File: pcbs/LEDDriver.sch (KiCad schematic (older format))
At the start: 1 part, among them J1 Conn_02x32_Counter_Clockwise

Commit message: LED driver part done.
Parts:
- added C1: 10n, Resistors_SMD:R_0603, symbol C
- added C2: 100n, Resistors_SMD:R_0603, symbol C
- added C3: 10u, Resistors_SMD:R_0603, symbol C
- added J2: Conn_02x03_Odd_Even, Pin_Headers:Pin_Header_Straight_2x03_Pitch2.54mm, symbol Conn_02x03_Odd_Even
- added R1, R2: 0R, Resistors_SMD:R_0603, symbol R
- added R3, R4: 10k, Resistors_SMD:R_0603, symbol R
- added RV1: T73YE103KT20, Potis:Vishay_T73YE103KT20, symbol POT
- added U1: DAC101C085, SSOP:VSSOP-8_3.0x3.0mm_Pitch0.65mm, symbol DAC101C085
- J1: footprint (none) -> Pin_Headers:Pin_Header_Straight_2x32_Pitch2.54mm; Samtec (none) -> TSW-132-07-G-D
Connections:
- net LED_N_01: now reaches J1.1 (Pin_1)
- net LED_N_10: now reaches J1.10 (Pin_10)
- net LED_N_11: now reaches J1.11 (Pin_11)
- net LED_N_12: now reaches J1.12 (Pin_12)
- net LED_N_13: now reaches J1.13 (Pin_13)
- net LED_N_14: now reaches J1.14 (Pin_14)
- net LED_N_15: now reaches J1.15 (Pin_15)
- net LED_N_16: now reaches J1.16 (Pin_16)
- net LED_N_17: now reaches J1.17 (Pin_17)
- net LED_N_18: now reaches J1.18 (Pin_18)
- net LED_N_19: now reaches J1.19 (Pin_19)
- net LED_N_02: now reaches J1.2 (Pin_2)
- net LED_N_20: now reaches J1.20 (Pin_20)
- net LED_N_21: now reaches J1.21 (Pin_21)
- net LED_N_22: now reaches J1.22 (Pin_22)
- net LED_N_23: now reaches J1.23 (Pin_23)
- net LED_N_24: now reaches J1.24 (Pin_24)
- net LED_N_25: now reaches J1.25 (Pin_25)
- net LED_N_26: now reaches J1.26 (Pin_26)
- net LED_N_27: now reaches J1.27 (Pin_27)
- net LED_N_28: now reaches J1.28 (Pin_28)
- net LED_N_29: now reaches J1.29 (Pin_29)
- net LED_N_03: now reaches J1.3 (Pin_3)
- net LED_N_30: now reaches J1.30 (Pin_30)
- net LED_N_31: now reaches J1.31 (Pin_31)
- net LED_N_32: now reaches J1.32 (Pin_32)
- net LED_N_33: now reaches J1.33 (Pin_33)
- net LED_N_34: now reaches J1.34 (Pin_34)
- net LED_N_35: now reaches J1.35 (Pin_35)
- net LED_N_36: now reaches J1.36 (Pin_36)
- net LED_N_37: now reaches J1.37 (Pin_37)
- net LED_N_38: now reaches J1.38 (Pin_38)
- net LED_N_39: now reaches J1.39 (Pin_39)
- net LED_N_04: now reaches J1.4 (Pin_4)
- net LED_N_40: now reaches J1.40 (Pin_40)
- net LED_N_41: now reaches J1.41 (Pin_41)
- net LED_N_42: now reaches J1.42 (Pin_42)
- net LED_N_43: now reaches J1.43 (Pin_43)
- net LED_N_44: now reaches J1.44 (Pin_44)
- net LED_N_45: now reaches J1.45 (Pin_45)
- net LED_N_46: now reaches J1.46 (Pin_46)
- net LED_N_47: now reaches J1.47 (Pin_47)
- net LED_N_48: now reaches J1.48 (Pin_48)
- net LED_N_49: now reaches J1.49 (Pin_49)
- net LED_N_05: now reaches J1.5 (Pin_5)
- net LED_N_50: now reaches J1.50 (Pin_50)
- net LED_N_51: now reaches J1.51 (Pin_51)
- net LED_N_52: now reaches J1.52 (Pin_52)
- net LED_N_53: now reaches J1.53 (Pin_53)
- net LED_N_54: now reaches J1.54 (Pin_54)
- net LED_N_55: now reaches J1.55 (Pin_55)
- net LED_N_56: now reaches J1.56 (Pin_56)
- net LED_N_57: now reaches J1.57 (Pin_57)
- net LED_N_58: now reaches J1.58 (Pin_58)
- net LED_N_59: now reaches J1.59 (Pin_59)
- net LED_N_06: now reaches J1.6 (Pin_6)
- net LED_N_60: now reaches J1.60 (Pin_60)
- net LED_N_61: now reaches J1.61 (Pin_61)
- net LED_N_62: now reaches J1.62 (Pin_62)
- net LED_N_63: now reaches J1.63 (Pin_63)
- net LED_N_64: now reaches J1.64 (Pin_64)
- net LED_N_07: now reaches J1.7 (Pin_7)
- net LED_N_08: now reaches J1.8 (Pin_8)
- net LED_N_09: now reaches J1.9 (Pin_9)
- new net: R1.2, U1.1 (ADR0)
- new net: R2.2, U1.2 (ADR1)
- new net: R3.1, RV1.1
- new net: J2.1 (Pin_1), RV1.2
- new net 3V3: C1.1, C2.1, C3.1, R1.1, R2.1, R3.2, U1.6 (VA), U1.7 (VREF)
- new net GND: C1.2, C2.2, C3.2, J2.5 (Pin_5), R4.2, RV1.3, U1.5 (GND)
- new net I2C_SCL: U1.4 (SDA)
- new net I2C_SDA: U1.3 (SCL)
- new net VDAC: J2.3 (Pin_3), U1.8 (VOUT)
- new net VSIG: J2.2 (Pin_2), J2.4 (Pin_4), J2.6 (Pin_6), R4.1
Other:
- moved on the sheet: J1

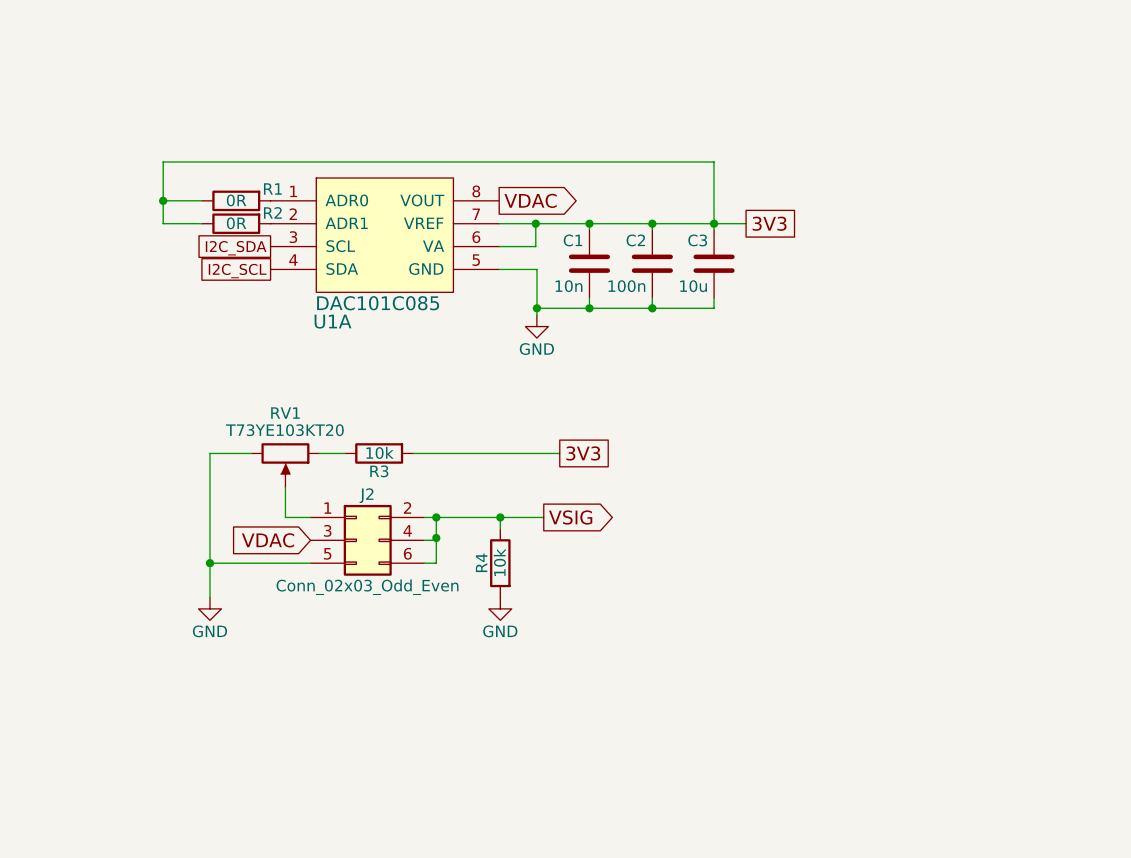
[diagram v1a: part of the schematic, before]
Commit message: Only UI is left for schematics.
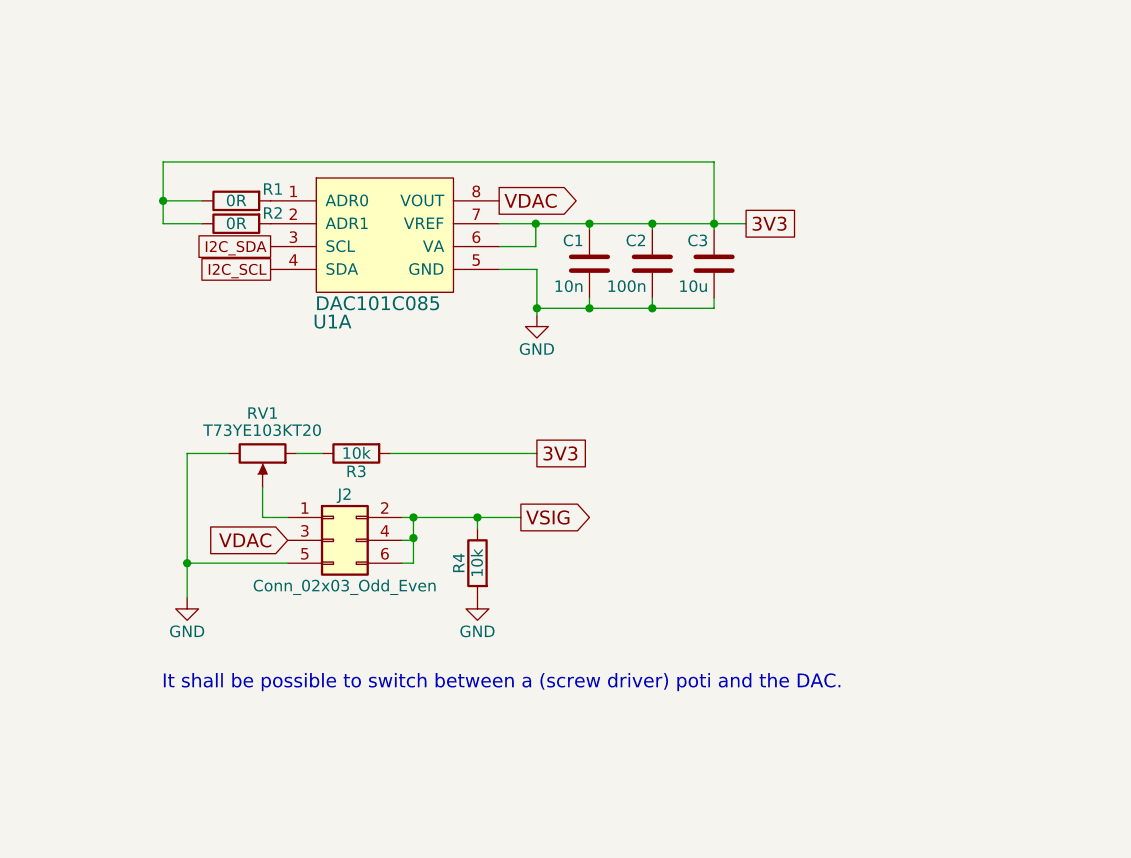
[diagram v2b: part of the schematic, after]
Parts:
- C1: Digikey 490-7194-1-ND -> 311-1085-1-ND
- C2: Digikey 490-5881-1-ND -> 311-1088-1-ND
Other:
- note added: "It shall be possible to switch between a (screw driver) poti and the DAC."
- moved on the sheet: J2, R3, R4, RV1
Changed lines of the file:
@@
 LIBS:myopamps
 LIBS:mydacs
+LIBS:mydcdcs
 LIBS:led_driver-cache
 EELAYER 25 0
@@
 $Descr A4 11693 8268
 encoding utf-8
-Sheet 2 35
+Sheet 2 37
 Title "UV LED Driver with 64 Stages and DAC"
 Date "2017-11-13"
@@
 F 2 "Resistors_SMD:R_0603" H 9733 3150 50  0001 C CNN
 F 3 "" H 9695 3300 50  0000 C CNN
-F 4 "490-5881-1-ND" H 9695 3300 60  0001 C CNN "Digikey"
+F 4 "311-1088-1-ND" H 9695 3300 60  0001 C CNN "Digikey"
 	1    9695 3300
 	-1   0    0    -1
 $EndComp
-$Comp
-L C C1
-U 1 1 5A10F0A2
-P 9420 3300
-F 0 "C1" H 9445 3400 50  0000 L CNN
-F 1 "10n" H 9445 3200 50  0000 L CNN
-F 2 "Resistors_SMD:R_0603" H 9458 3150 50  0001 C CNN
-F 3 "" H 9420 3300 50  0000 C CNN
-F 4 "490-7194-1-ND" H 9420 3300 60  0001 C CNN "Digikey"
-	1    9420 3300
-	-1   0    0    -1
-$EndComp
-Wire Wire Line
-	9025 3125 9185 3125
-Wire Wire Line
-	9185 3125 9420 3125
-Wire Wire Line
-	9420 3125 9695 3125
-Wire Wire Line
-	9695 3125 9965 3125
-Wire Wire Line
-	9965 3125 10105 3125
+Wire Wire Line
+	9025 3125 10105 3125
 Wire Wire Line
 	9695 3125 9695 3150
@@
 	9025 3325 9190 3325
 Wire Wire Line
-	9190 3325 9190 3495
-Wire Wire Line
-	9190 3495 9190 3525
+	9190 3325 9190 3525
 Wire Wire Line
 	9695 3495 9695 3450
 Wire Wire Line
-	9190 3495 9420 3495
-Wire Wire Line
-	9420 3495 9695 3495
-Wire Wire Line
-	9695 3495 9965 3495
+	9190 3495 9965 3495
 Connection ~ 9190 3495
 Wire Wire Line
@@
 Connection ~ 9695 3495
 Wire Wire Line
-	9965 2855 9965 3125
-Wire Wire Line
-	9965 3125 9965 3150
+	9965 2855 9965 3150
 Connection ~ 9965 3125
 Text GLabel 8025 3225 0    47   UnSpc ~ 0
@@
 	7555 3125 7725 3125
 Wire Wire Line
-	7555 2855 7555 3025
-Wire Wire Line
-	7555 3025 7555 3125
+	7555 2855 7555 3125
 Wire Wire Line
 	7725 3025 7555 3025
@@
 L R R3
 U 1 1 5A1370E7
-P 8500 4130
-F 0 "R3" V 8580 4130 50  0000 C CNN
-F 1 "10k" V 8500 4130 50  0000 C CNN
-F 2 "Resistors_SMD:R_0603" V 8430 4130 50  0001 C CNN
-F 3 "" H 8500 4130 50  0001 C CNN
-F 4 "311-10KGRCT-ND" V 8500 4130 60  0001 C CNN "Digikey"
-	1    8500 4130
+P 8400 4130
+F 0 "R3" V 8480 4130 50  0000 C CNN
+F 1 "10k" V 8400 4130 50  0000 C CNN
+F 2 "Resistors_SMD:R_0603" V 8330 4130 50  0001 C CNN
+F 3 "" H 8400 4130 50  0001 C CNN
+F 4 "311-10KGRCT-ND" V 8400 4130 60  0001 C CNN "Digikey"
+	1    8400 4130
 	0    -1   1    0
 $EndComp
-Text GLabel 9290 4130 2    60   UnSpc ~ 0
+Text GLabel 9190 4130 2    60   UnSpc ~ 0
 3V3
 Wire Wire Line
-	8650 4130 9290 4130
-Wire Wire Line
-	8350 4130 8240 4130
-Wire Wire Line
-	8200 4410 8090 4410
-Wire Wire Line
-	8090 4410 8090 4280
+	8550 4130 9190 4130
+Wire Wire Line
+	8250 4130 8140 4130
+Wire Wire Line
+	8100 4410 7990 4410
+Wire Wire Line
+	7990 4410 7990 4280
 $Comp
 L POT RV1
 U 1 1 5A139EFD
-P 8090 4130
-F 0 "RV1" V 7915 4130 50  0000 C CNN
-F 1 "T73YE103KT20" V 7990 4130 50  0000 C CNN
-F 2 "Potis:Vishay_T73YE103KT20" H 8090 4130 50  0001 C CNN
-F 3 "http://www.bourns.com/docs/Product-Datasheets/3362.pdf" H 8090 4130 50  0001 C CNN
-F 4 " 3362R-103LF-ND" V 8090 4130 60  0001 C CNN "Digikey"
-	1    8090 4130
+P 7990 4130
+F 0 "RV1" V 7815 4130 50  0000 C CNN
+F 1 "T73YE103KT20" V 7890 4130 50  0000 C CNN
+F 2 "Potis:Vishay_T73YE103KT20" H 7990 4130 50  0001 C CNN
+F 3 "http://www.bourns.com/docs/Product-Datasheets/3362.pdf" H 7990 4130 50  0001 C CNN
+F 4 " 3362R-103LF-ND" V 7990 4130 60  0001 C CNN "Digikey"
+	1    7990 4130
 	0    1    1    0
 $EndComp
@@
 L GND #PWR1
 U 1 1 5A142088
-P 7760 4760
-F 0 "#PWR1" H 7760 4510 50  0001 C CNN
-F 1 "GND" H 7760 4610 50  0000 C CNN
-F 2 "" H 7760 4760 50  0000 C CNN
-F 3 "" H 7760 4760 50  0000 C CNN
-	1    7760 4760
+P 7660 4760
+F 0 "#PWR1" H 7660 4510 50  0001 C CNN
+F 1 "GND" H 7660 4610 50  0000 C CNN
+F 2 "" H 7660 4760 50  0000 C CNN
+F 3 "" H 7660 4760 50  0000 C CNN
+	1    7660 4760
 	-1   0    0    -1
 $EndComp
-Text GLabel 8200 4510 0    60   Input ~ 0
+Text GLabel 8100 4510 0    60   Input ~ 0
 VDAC
-Text GLabel 9220 4410 2    60   Output ~ 0
+Text GLabel 9120 4410 2    60   Output ~ 0
 VSIG
 Wire Wire Line
-	8700 4410 8750 4410
-Wire Wire Line
-	8750 4410 9030 4410
-Wire Wire Line
-	9030 4410 9220 4410
-Wire Wire Line
-	8750 4510 8700 4510
-Wire Wire Line
-	8750 4410 8750 4500
-Wire Wire Line
-	8750 4500 8750 4510
-Connection ~ 8750 4410
+	8600 4410 9120 4410
+Wire Wire Line
+	8650 4510 8600 4510
+Wire Wire Line
+	8650 4410 8650 4510
+Connection ~ 8650 4410
 $Comp
 L Conn_02x03_Odd_Even J2
 U 1 1 5A1548D7
-P 8400 4510
-F 0 "J2" H 8450 4710 50  0000 C CNN
-F 1 "Conn_02x03_Odd_Even" H 8450 4310 50  0000 C CNN
-F 2 "Pin_Headers:Pin_Header_Straight_2x03_Pitch2.54mm" H 8400 4510 50  0001 C CNN
-F 3 "" H 8400 4510 50  0001 C CNN
-F 4 "TSW-103-07-G-D" H 8400 4510 60  0001 C CNN "Digikey"
-	1    8400 4510
+P 8300 4510
+F 0 "J2" H 8350 4710 50  0000 C CNN
+F 1 "Conn_02x03_Odd_Even" H 8350 4310 50  0000 C CNN
+F 2 "Pin_Headers:Pin_Header_Straight_2x03_Pitch2.54mm" H 8300 4510 50  0001 C CNN
+F 3 "" H 8300 4510 50  0001 C CNN
+F 4 "TSW-103-07-G-D" H 8300 4510 60  0001 C CNN "Digikey"
+	1    8300 4510
 	1    0    0    -1
 $EndComp
 Wire Wire Line
-	8700 4610 8750 4610
-Wire Wire Line
-	8750 4610 8750 4500
-Connection ~ 8750 4500
-Wire Wire Line
-	8200 4610 7760 4610
-Wire Wire Line
-	7760 4130 7760 4610
-Wire Wire Line
-	7760 4610 7760 4760
-Wire Wire Line
-	7760 4130 7940 4130
-Connection ~ 7760 4610
+	8600 4610 8650 4610
+Wire Wire Line
+	8650 4610 8650 4500
+Connection ~ 8650 4500
+Wire Wire Line
+	8100 4610 7660 4610
+Wire Wire Line
+	7660 4130 7660 4760
+Wire Wire Line
+	7660 4130 7840 4130
+Connection ~ 7660 4610
 $Comp
 L R R4
 U 1 1 5A15A992
-P 9030 4610
-F 0 "R4" V 9110 4610 50  0000 C CNN
-F 1 "10k" V 9030 4610 50  0000 C CNN
-F 2 "Resistors_SMD:R_0603" V 8960 4610 50  0001 C CNN
-F 3 "" H 9030 4610 50  0001 C CNN
-F 4 "311-10KGRCT-ND" V 9030 4610 60  0001 C CNN "Digikey"
-	1    9030 4610
+P 8930 4610
+F 0 "R4" V 9010 4610 50  0000 C CNN
+F 1 "10k" V 8930 4610 50  0000 C CNN
+F 2 "Resistors_SMD:R_0603" V 8860 4610 50  0001 C CNN
+F 3 "" H 8930 4610 50  0001 C CNN
+F 4 "311-10KGRCT-ND" V 8930 4610 60  0001 C CNN "Digikey"
+	1    8930 4610
 	-1   0    0    -1
 $EndComp
 Wire Wire Line
-	9030 4460 9030 4410
-Connection ~ 9030 4410
+	8930 4460 8930 4410
+Connection ~ 8930 4410
 $Comp
 L GND #PWR2
 U 1 1 5A15B686
-P 9030 4760
-F 0 "#PWR2" H 9030 4510 50  0001 C CNN
-F 1 "GND" H 9030 4610 50  0000 C CNN
-F 2 "" H 9030 4760 50  0000 C CNN
-F 3 "" H 9030 4760 50  0000 C CNN
-	1    9030 4760
+P 8930 4760
+F 0 "#PWR2" H 8930 4510 50  0001 C CNN
+F 1 "GND" H 8930 4610 50  0000 C CNN
+F 2 "" H 8930 4760 50  0000 C CNN
+F 3 "" H 8930 4760 50  0000 C CNN
+	1    8930 4760
 	-1   0    0    -1
 $EndComp
+Text Notes 7550 5170 0    60   ~ 0
+It shall be possible to switch between a (screw driver) poti and the DAC.
+$Comp
+L C C1
+U 1 1 5A10F0A2
+P 9420 3300
+F 0 "C1" H 9445 3400 50  0000 L CNN
+F 1 "10n" H 9445 3200 50  0000 L CNN
+F 2 "Resistors_SMD:R_0603" H 9458 3150 50  0001 C CNN
+F 3 "" H 9420 3300 50  0000 C CNN
+F 4 "311-1085-1-ND" H 9420 3300 60  0001 C CNN "Digikey"
+	1    9420 3300
+	-1   0    0    -1
+$EndComp

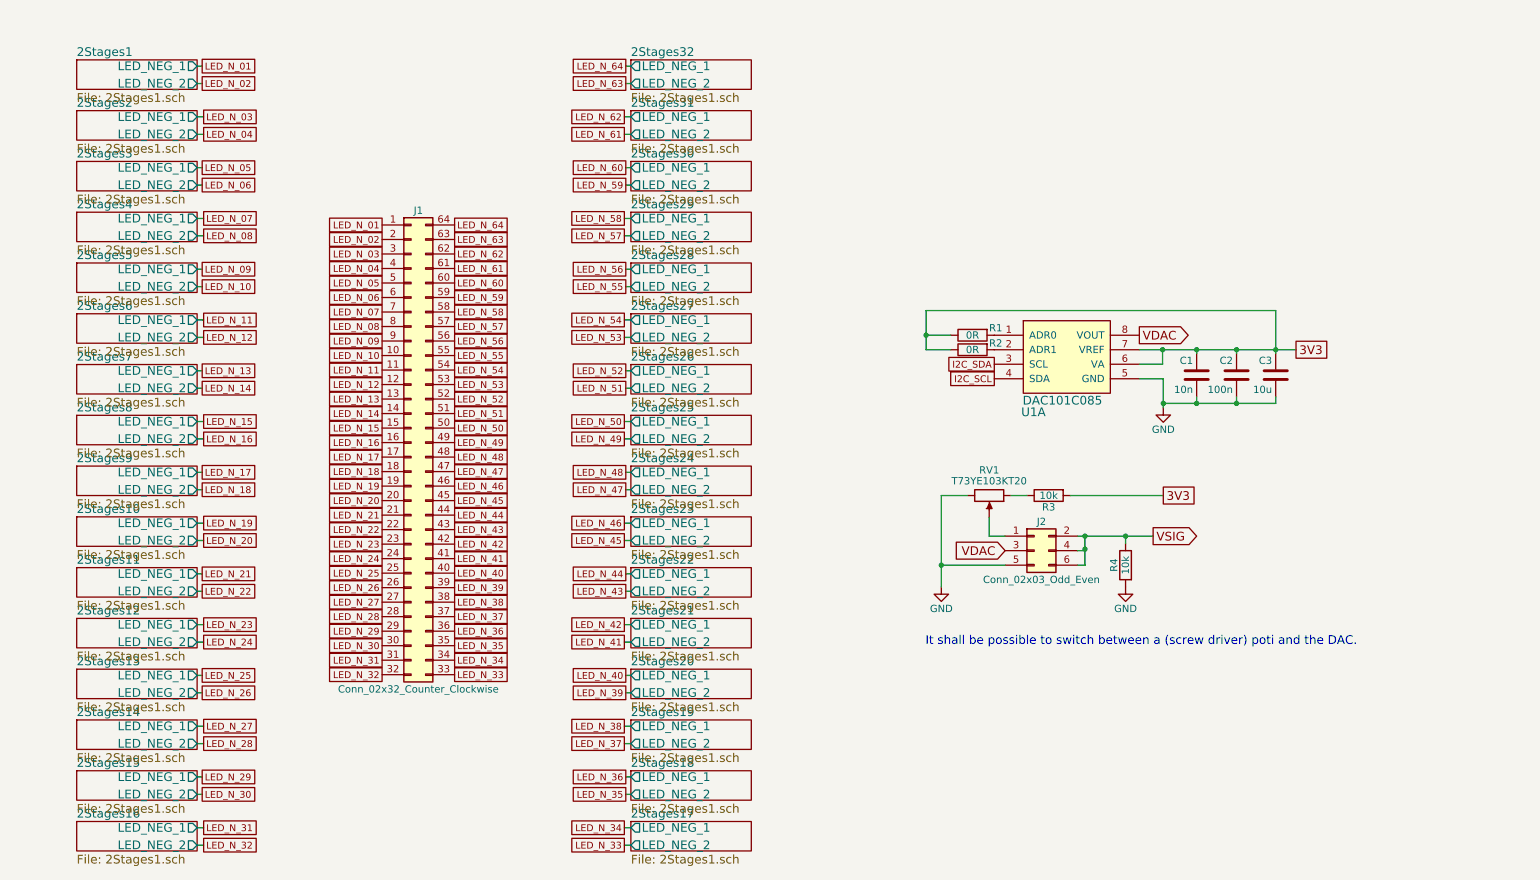
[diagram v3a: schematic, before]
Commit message: No DRC errors anymore in schematics.
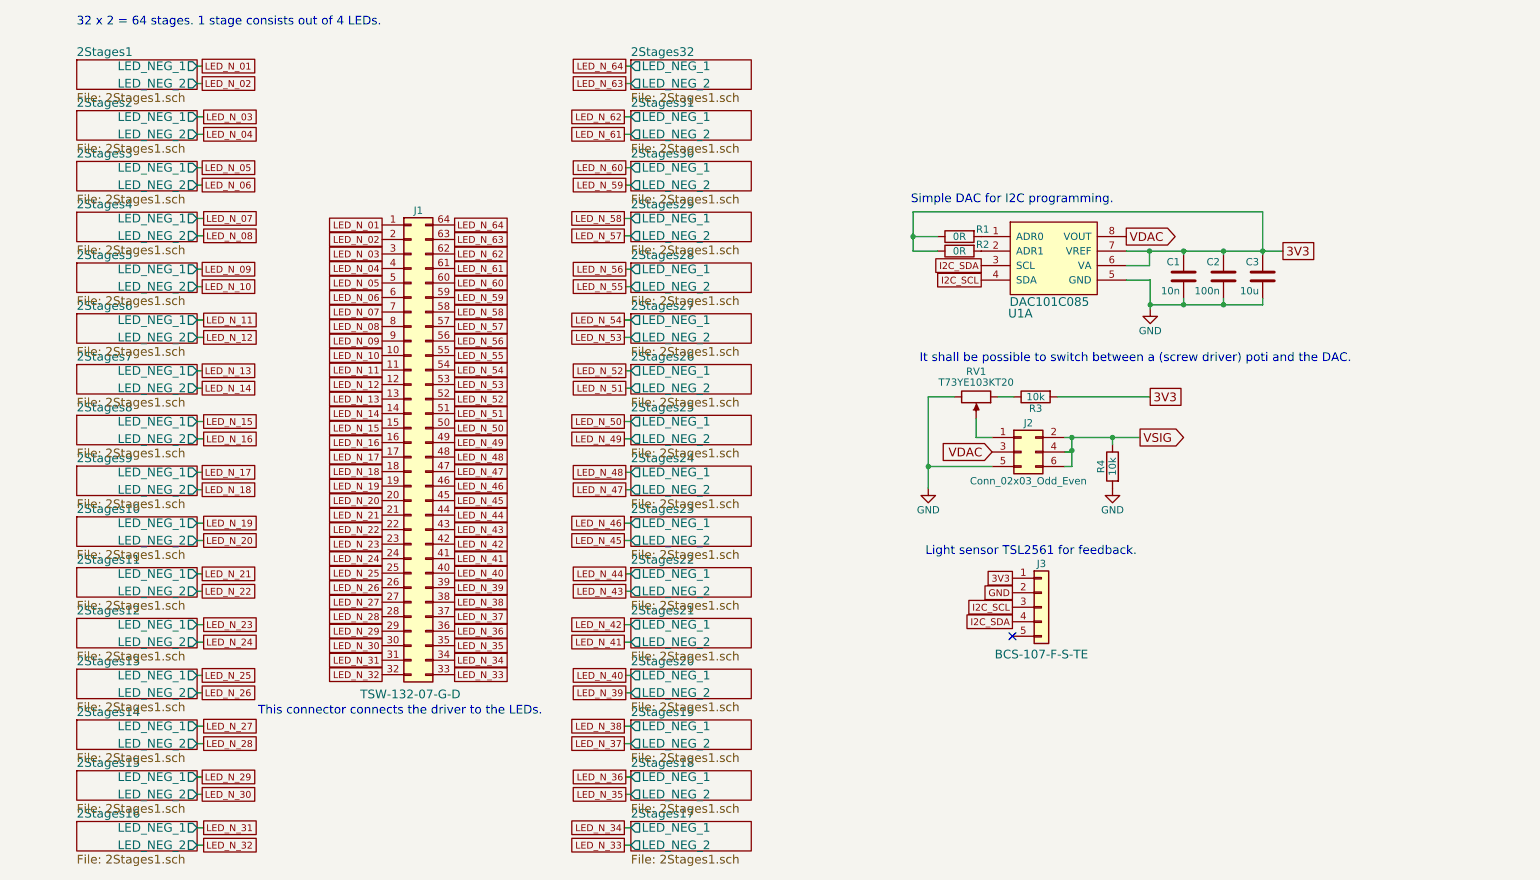
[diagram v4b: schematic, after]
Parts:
- added J3: Conn_01x05, Pin_Headers:Pin_Header_Straight_1x05_Pitch2.54mm, symbol Conn_01x05
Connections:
- net 3V3: now also J3.1 (Pin_1)
- net GND: now also J3.2 (Pin_2)
- net I2C_SCL: now also J3.3 (Pin_3)
- net I2C_SDA: now also J3.4 (Pin_4)
- no-connect marks 0 -> 1
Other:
- note added: "32 x 2 = 64 stages. 1 stage consists out of 4 LEDs."
- note added: "Light sensor TSL2561 for feedback."
- note added: "Simple DAC for I2C programming."
- note added: "This connector connects the driver to the LEDs."
- moved on the sheet: C1, C2, C3, J2, R1, R2, R3, R4, RV1, U1A
